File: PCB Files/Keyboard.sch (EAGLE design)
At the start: 78 parts

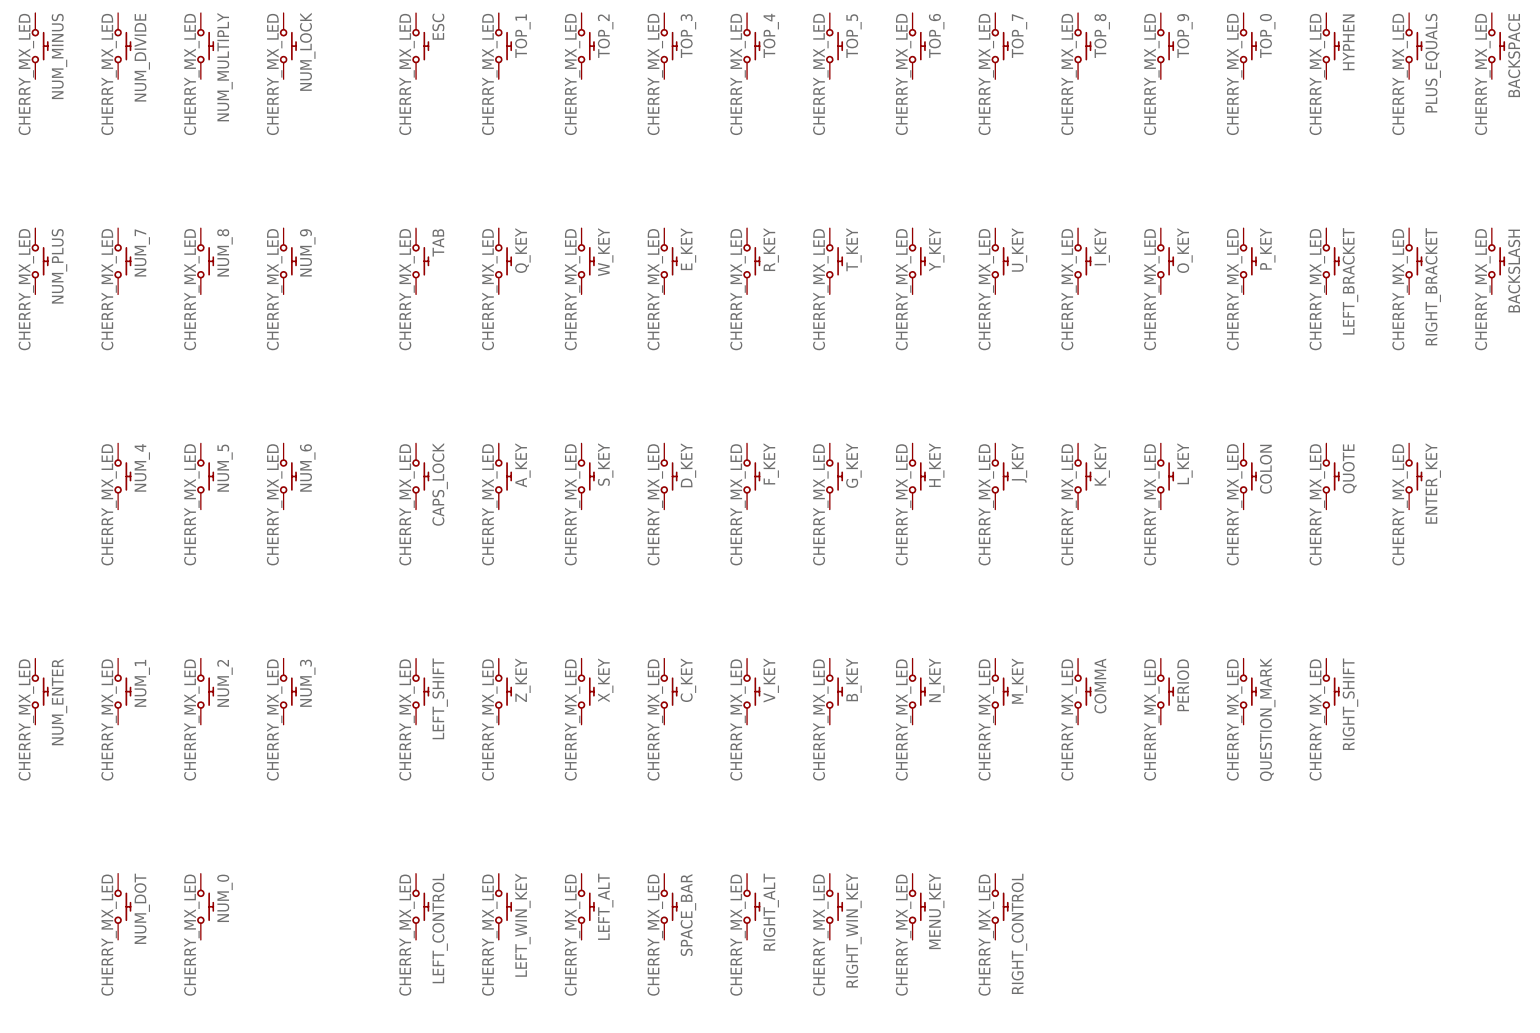
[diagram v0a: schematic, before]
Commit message: Added Teensy Pinout, Teensy Eagle Files, Plate CAD layouts and started pcb schematic
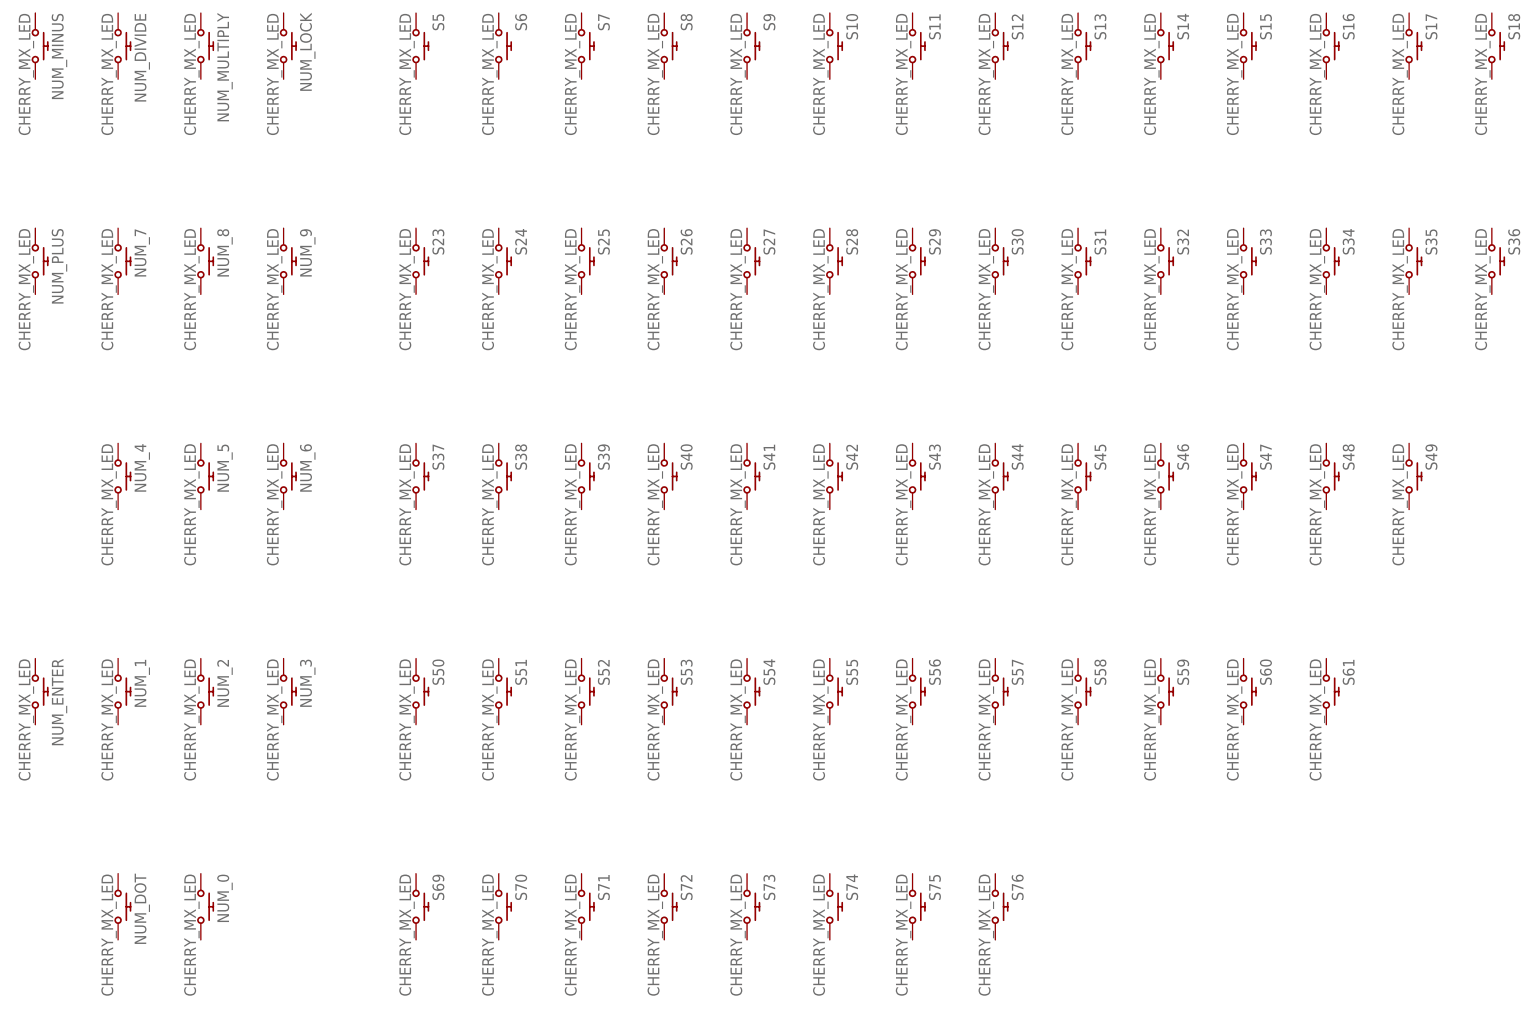
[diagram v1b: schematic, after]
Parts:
- renumbered A_KEY to S38, BACKSLASH to S36, BACKSPACE to S18, B_KEY to S55, CAPS_LOCK to S37, COLON to S47, COMMA to S58, C_KEY to S53, D_KEY to S40, ENTER_KEY to S49, ESC to S5, E_KEY to S26, F_KEY to S41, G_KEY to S42, HYPHEN to S16, H_KEY to S43, I_KEY to S31, J_KEY to S44, K_KEY to S45, LEFT_ALT to S71, LEFT_BRACKET to S34, LEFT_CONTROL to S69, LEFT_SHIFT to S50, LEFT_WIN_KEY to S70, L_KEY to S46, MENU_KEY to S75, M_KEY to S57, N_KEY to S56, O_KEY to S32, PERIOD to S59, PLUS_EQUALS to S17, P_KEY to S33, QUESTION_MARK to S60, QUOTE to S48, Q_KEY to S24, RIGHT_ALT to S73, RIGHT_BRACKET to S35, RIGHT_CONTROL to S76, RIGHT_SHIFT to S61, RIGHT_WIN_KEY to S74, R_KEY to S27, SPACE_BAR to S72, S_KEY to S39, TAB to S23, TOP_0 to S15, TOP_1 to S6, TOP_2 to S7, TOP_3 to S8, TOP_4 to S9, TOP_5 to S10, TOP_6 to S11, TOP_7 to S12, TOP_8 to S13, TOP_9 to S14, T_KEY to S28, U_KEY to S30, V_KEY to S54, W_KEY to S25, X_KEY to S52, Y_KEY to S29, Z_KEY to S51
